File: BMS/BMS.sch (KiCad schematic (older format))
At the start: 77 parts, among them J1 Cell Taps, J10 Current Sensor, J2 IsoSPI, J3 Temp 1, J4 Temp 2, J5 Temp 3, J6 Temp 4, J7 Temp 5, J8 Temp 6, J9 Temp 7, Q1 NSV1C201MZ4, Q2 BSS308PE, Q3 BSS308PE, Q4 BSS308PE, Q5 BSS308PE, Q6 BSS308PE, Q7 BSS308PE, Q8 BSS308PE, SW1 SW_DIP_x04, U1 LTC6811, U2 ADG708

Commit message: Begin work on BMS schematic
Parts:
- U1: symbol BMS-rescue:LTC6811-FS_FINAL -> FS_FINAL:LTC6811
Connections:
- wire segments 233 -> 230
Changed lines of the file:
@@
 EESchema Schematic File Version 4
-LIBS:symbols
-LIBS:arduino
-LIBS:FS FINAL
-LIBS:BMS-cache
 EELAYER 26 0
 EELAYER END
@@
 $EndDescr
 $Comp
-L BMS-rescue:LTC6811-FS_FINAL U1
+L FS_FINAL:LTC6811 U1
 U 1 1 5C45220C
 P 5800 1100
@@
 	6500 3200 7100 3200
 Wire Wire Line
-	7500 3500 7100 3500
-Wire Wire Line
 	6500 3100 7500 3100
 Wire Wire Line
@@
 Wire Wire Line
 	5000 3900 5000 6750
-Wire Wire Line
-	7600 3500 7500 3500
-Connection ~ 7500 3500
 Text GLabel 5100 6750 2    50   Output ~ 0
 V-
@@
 Wire Wire Line
 	7950 2150 7850 2150
-Connection ~ 7850 2150
 Text GLabel 7700 4350 0    50   Input ~ 0
 MUX_A0
@@
 Text GLabel 8500 5350 2    50   Output ~ 0
 TEMP
-Wire Wire Line
-	8850 2250 8950 2250
-Wire Wire Line
-	8850 2850 8950 2850
-Connection ~ 8950 2250
-Connection ~ 8950 2850
 $Comp
 L FS_FINAL:HM2113ZNL L1
@@
 	1    0    0    -1
 $EndComp
-Wire Wire Line
-	8950 2250 9150 2250
-Wire Wire Line
-	8950 2850 9150 2850
 Wire Wire Line
 	9150 2250 9150 2450
@@
 Wire Wire Line
 	10450 2650 10250 2650
+Wire Wire Line
+	7100 3500 7600 3500
+Wire Wire Line
+	8850 2250 9150 2250
+Wire Wire Line
+	8850 2850 9150 2850
 $EndSCHEMATC

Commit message: BMS again
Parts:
- C13, C14: value 1uF -> 10nF
- R17: value 1M -> 10k
- R33, R34, R35, R36, R37, R38, R39: value R -> 10k
- SW1: footprint Buttons_Switches_SMD:SW_DIP_x4_W8.61mm_Slide_LowProfile -> FSFootprints:DIP A6H-4101
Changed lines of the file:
@@
 EESchema Schematic File Version 4
+LIBS:BMS-cache
 EELAYER 26 0
 EELAYER END
@@
 F 0 "SW1" H 10300 1617 50  0000 C CNN
 F 1 "SW_DIP_x04" H 10300 1526 50  0000 C CNN
-F 2 "Buttons_Switches_SMD:SW_DIP_x4_W8.61mm_Slide_LowProfile" H 10300 1150 50  0001 C CNN
-F 3 "" H 10300 1150 50  0001 C CNN
+F 2 "FSFootprints:DIP A6H-4101" H 10300 1150 50  0001 C CNN
+F 3 "https://omronfs.omron.com/en_US/ecb/products/pdf/en-a6h.pdf" H 10300 1150 50  0001 C CNN
 	1    10300 1150
 	1    0    0    -1
@@
 P 6650 2800
 F 0 "R17" V 6750 2800 50  0000 C CNN
-F 1 "1M" V 6650 2800 50  0000 C CNN
+F 1 "10k" V 6650 2800 50  0000 C CNN
 F 2 "Resistors_SMD:R_0805_HandSoldering" V 6580 2800 50  0001 C CNN
 F 3 "~" H 6650 2800 50  0001 C CNN
@@
 P 6100 4600
 F 0 "R34" H 6030 4554 50  0000 R CNN
-F 1 "R" H 6030 4645 50  0000 R CNN
+F 1 "10k" H 6030 4645 50  0000 R CNN
 F 2 "Resistors_SMD:R_0805_HandSoldering" V 6030 4600 50  0001 C CNN
 F 3 "~" H 6100 4600 50  0001 C CNN
@@
 P 6300 4600
 F 0 "R35" H 6230 4554 50  0000 R CNN
-F 1 "R" H 6230 4645 50  0000 R CNN
+F 1 "10k" H 6230 4645 50  0000 R CNN
 F 2 "Resistors_SMD:R_0805_HandSoldering" V 6230 4600 50  0001 C CNN
 F 3 "~" H 6300 4600 50  0001 C CNN
@@
 P 6500 4600
 F 0 "R36" H 6430 4554 50  0000 R CNN
-F 1 "R" H 6430 4645 50  0000 R CNN
+F 1 "10k" H 6430 4645 50  0000 R CNN
 F 2 "Resistors_SMD:R_0805_HandSoldering" V 6430 4600 50  0001 C CNN
 F 3 "~" H 6500 4600 50  0001 C CNN
@@
 P 6700 4600
 F 0 "R37" H 6630 4554 50  0000 R CNN
-F 1 "R" H 6630 4645 50  0000 R CNN
+F 1 "10k" H 6630 4645 50  0000 R CNN
 F 2 "Resistors_SMD:R_0805_HandSoldering" V 6630 4600 50  0001 C CNN
 F 3 "~" H 6700 4600 50  0001 C CNN
@@
 P 5900 4600
 F 0 "R33" H 5830 4554 50  0000 R CNN
-F 1 "R" H 5830 4645 50  0000 R CNN
+F 1 "10k" H 5830 4645 50  0000 R CNN
 F 2 "Resistors_SMD:R_0805_HandSoldering" V 5830 4600 50  0001 C CNN
 F 3 "~" H 5900 4600 50  0001 C CNN
@@
 P 6900 4600
 F 0 "R38" H 6830 4554 50  0000 R CNN
-F 1 "R" H 6830 4645 50  0000 R CNN
+F 1 "10k" H 6830 4645 50  0000 R CNN
 F 2 "Resistors_SMD:R_0805_HandSoldering" V 6830 4600 50  0001 C CNN
 F 3 "~" H 6900 4600 50  0001 C CNN
@@
 P 7100 4600
 F 0 "R39" H 7030 4554 50  0000 R CNN
-F 1 "R" H 7030 4645 50  0000 R CNN
+F 1 "10k" H 7030 4645 50  0000 R CNN
 F 2 "Resistors_SMD:R_0805_HandSoldering" V 7030 4600 50  0001 C CNN
 F 3 "~" H 7100 4600 50  0001 C CNN
@@
 P 9250 3050
 F 0 "C13" V 9350 3050 50  0000 C CNN
-F 1 "1uF" V 9150 3050 50  0000 C CNN
+F 1 "10nF" V 9150 3050 50  0000 C CNN
 F 2 "Capacitors_SMD:C_0805_HandSoldering" H 9288 2900 50  0001 C CNN
 F 3 "~" H 9250 3050 50  0001 C CNN
@@
 P 10350 3050
 F 0 "C14" V 10450 3050 50  0000 C CNN
-F 1 "1uF" V 10250 3050 50  0000 C CNN
+F 1 "10nF" V 10250 3050 50  0000 C CNN
 F 2 "Capacitors_SMD:C_0805_HandSoldering" H 10388 2900 50  0001 C CNN
 F 3 "~" H 10350 3050 50  0001 C CNN

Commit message: BMS board v0.1
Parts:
- removed J10: Current Sensor, Connectors_Molex:Molex_NanoFit_1x03x2.50mm_Straight, symbol Connector:Conn_01x03_Male
- J1: footprint FSFootprints:Cell Taps -> Connectors_Molex:Molex_NanoFit_1x08x2.50mm_Straight
- R17: value 10k -> 0
- U1: footprint Housings_SSOP:SSOP-48_7.5x15.9mm_Pitch0.635mm -> FSFootprints:FSOP-48_[LTC6811-2]
- U2: footprint Package_SO:TSSOP-16_4.4x5mm_P0.65mm -> Housings_SSOP:TSSOP-16_4.4x5mm_Pitch0.65mm
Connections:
- wire segments 230 -> 232
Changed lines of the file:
@@
 F 0 "U1" H 5800 1265 50  0000 C CNN
 F 1 "LTC6811" H 5800 1174 50  0000 C CNN
-F 2 "Housings_SSOP:SSOP-48_7.5x15.9mm_Pitch0.635mm" H 5800 1100 50  0001 C CNN
+F 2 "FSFootprints:FSOP-48_[LTC6811-2]" H 5800 1100 50  0001 C CNN
 F 3 "" H 5800 1100 50  0001 C CNN
 	1    5800 1100
@@
 F 0 "J1" H 906 1728 50  0000 C CNN
 F 1 "Cell Taps" V 700 1200 50  0000 C CNN
-F 2 "FSFootprints:Cell Taps" H 800 1250 50  0001 C CNN
+F 2 "Connectors_Molex:Molex_NanoFit_1x08x2.50mm_Straight" H 800 1250 50  0001 C CNN
 F 3 "~" H 800 1250 50  0001 C CNN
 	1    800  1250
@@
 	1    7100 3350
 	-1   0    0    1
-$EndComp
-$Comp
-L Device:R R17
-U 1 1 5C72E4D4
-P 6650 2800
-F 0 "R17" V 6750 2800 50  0000 C CNN
-F 1 "10k" V 6650 2800 50  0000 C CNN
-F 2 "Resistors_SMD:R_0805_HandSoldering" V 6580 2800 50  0001 C CNN
-F 3 "~" H 6650 2800 50  0001 C CNN
-	1    6650 2800
-	0    1    1    0
 $EndComp
 $Comp
@@
 Text GLabel 6500 2600 2    50   Input ~ 0
 VREG
-Text GLabel 6800 2800 2    50   Input ~ 0
-VREG
 Text GLabel 10800 950  2    50   Input ~ 0
 VREG
@@
 F 0 "U2" H 7800 5800 50  0000 L CNN
 F 1 "ADG708" H 7800 5700 50  0000 L CNN
-F 2 "Package_SO:TSSOP-16_4.4x5mm_P0.65mm" H 8350 4100 50  0001 L CNN
+F 2 "Housings_SSOP:TSSOP-16_4.4x5mm_Pitch0.65mm" H 8350 4100 50  0001 L CNN
 F 3 "https://www.analog.com/media/en/technical-documentation/data-sheets/ADG708_709.pdf" H 8110 4950 50  0001 C CNN
 	1    8100 4950
@@
 V-
 Text GLabel 5750 6150 2    50   Input ~ 0
-V-
-Text GLabel 7700 5550 0    50   Input ~ 0
 V-
 $Comp
@@
 Text GLabel 9250 3150 3    50   Input ~ 0
 V-
-$Comp
-L Connector:Conn_01x03_Male J10
-U 1 1 5C7A9370
-P 9800 3700
-F 0 "J10" H 9773 3723 50  0000 R CNN
-F 1 "Current Sensor" H 9773 3632 50  0000 R CNN
-F 2 "Connectors_Molex:Molex_NanoFit_1x03x2.50mm_Straight" H 9800 3700 50  0001 C CNN
-F 3 "~" H 9800 3700 50  0001 C CNN
-	1    9800 3700
-	-1   0    0    -1
-$EndComp
-Text GLabel 9600 3600 0    50   Input ~ 0
-VREG
-Text GLabel 9600 3800 0    50   Input ~ 0
-V-
-Wire Wire Line
-	9600 3700 6500 3700
 Text GLabel 7700 4650 0    50   Input ~ 0
 VREG
@@
 Text GLabel 7700 4550 0    50   Input ~ 0
 MUX_A2
-Text GLabel 6500 3400 2    50   Output ~ 0
+Text GLabel 6500 3500 2    50   Output ~ 0
 MUX_A0
-Text GLabel 6500 3500 2    50   Output ~ 0
+Text GLabel 6500 3800 2    50   Output ~ 0
 MUX_A1
-Text GLabel 6500 3600 2    50   Output ~ 0
+Text GLabel 6500 3700 2    50   Output ~ 0
 MUX_A2
-Text GLabel 6500 3800 2    50   Input ~ 0
+Text GLabel 6500 3400 2    50   Input ~ 0
 TEMP
 Text GLabel 8500 5350 2    50   Output ~ 0
@@
 	10450 2650 10250 2650
 Wire Wire Line
-	7100 3500 7600 3500
-Wire Wire Line
-	8850 2250 9150 2250
-Wire Wire Line
-	8850 2850 9150 2850
+	7100 3500 7500 3500
+Wire Wire Line
+	8850 2250 8950 2250
+Wire Wire Line
+	8850 2850 8950 2850
+Connection ~ 7500 3500
+Wire Wire Line
+	7500 3500 7600 3500
+Connection ~ 8950 2250
+Wire Wire Line
+	8950 2250 9150 2250
+Connection ~ 8950 2850
+Wire Wire Line
+	8950 2850 9150 2850
+Connection ~ 7850 2150
+Text GLabel 6500 3600 2    50   Input ~ 0
+VREG
+$Comp
+L Device:R R17
+U 1 1 5C80812D
+P 8200 850
+F 0 "R17" V 7993 850 50  0000 C CNN
+F 1 "0" V 8084 850 50  0000 C CNN
+F 2 "Resistors_SMD:R_0805_HandSoldering" V 8130 850 50  0001 C CNN
+F 3 "~" H 8200 850 50  0001 C CNN
+	1    8200 850
+	0    1    1    0
+$EndComp
+Text GLabel 8050 850  0    50   Output ~ 0
+VREG
+Text GLabel 8350 850  2    50   Output ~ 0
+VREG
 $EndSCHEMATC

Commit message: yikes
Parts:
- removed C14: 10nF, Capacitors_SMD:C_0805_HandSoldering, symbol Device:C_Small
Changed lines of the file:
@@
 Wire Wire Line
 	9250 2550 9350 2550
-$Comp
-L Device:R R40
-U 1 1 5CA16E1A
-P 10600 2450
-F 0 "R40" V 10700 2400 50  0000 L CNN
-F 1 "22" V 10600 2450 50  0000 C CNN
-F 2 "Resistors_SMD:R_0805_HandSoldering" V 10530 2450 50  0001 C CNN
-F 3 "~" H 10600 2450 50  0001 C CNN
-	1    10600 2450
-	0    1    -1   0
-$EndComp
-$Comp
-L Device:R R41
-U 1 1 5CA1723F
-P 10600 2650
-F 0 "R41" V 10700 2600 50  0000 L CNN
-F 1 "22" V 10600 2650 50  0000 C CNN
-F 2 "Resistors_SMD:R_0805_HandSoldering" V 10530 2650 50  0001 C CNN
-F 3 "~" H 10600 2650 50  0001 C CNN
-	1    10600 2650
-	0    1    -1   0
-$EndComp
 Wire Wire Line
 	10750 2450 10850 2450
@@
 Wire Wire Line
 	10850 2650 10750 2650
-$Comp
-L Device:C_Small C14
-U 1 1 5CA52F72
-P 10350 3050
-F 0 "C14" V 10450 3050 50  0000 C CNN
-F 1 "10nF" V 10250 3050 50  0000 C CNN
-F 2 "Capacitors_SMD:C_0805_HandSoldering" H 10388 2900 50  0001 C CNN
-F 3 "~" H 10350 3050 50  0001 C CNN
-	1    10350 3050
-	1    0    0    -1
-$EndComp
-Text GLabel 10350 3150 3    50   Input ~ 0
-V-
-Wire Wire Line
-	10350 2950 10350 2550
-Wire Wire Line
-	10250 2550 10350 2550
 Wire Wire Line
 	10250 2450 10450 2450
@@
 Text GLabel 8350 850  2    50   Output ~ 0
 VREG
+$Comp
+L Device:R R41
+U 1 1 5CA1723F
+P 10600 2650
+F 0 "R41" V 10700 2600 50  0000 L CNN
+F 1 "22" V 10600 2650 50  0000 C CNN
+F 2 "Resistors_SMD:R_0805_HandSoldering" V 10530 2650 50  0001 C CNN
+F 3 "~" H 10600 2650 50  0001 C CNN
+	1    10600 2650
+	0    1    -1   0
+$EndComp
+$Comp
+L Device:R R40
+U 1 1 5CA16E1A
+P 10600 2450
+F 0 "R40" V 10700 2400 50  0000 L CNN
+F 1 "22" V 10600 2450 50  0000 C CNN
+F 2 "Resistors_SMD:R_0805_HandSoldering" V 10530 2450 50  0001 C CNN
+F 3 "~" H 10600 2450 50  0001 C CNN
+	1    10600 2450
+	0    1    -1   0
+$EndComp
 $EndSCHEMATC

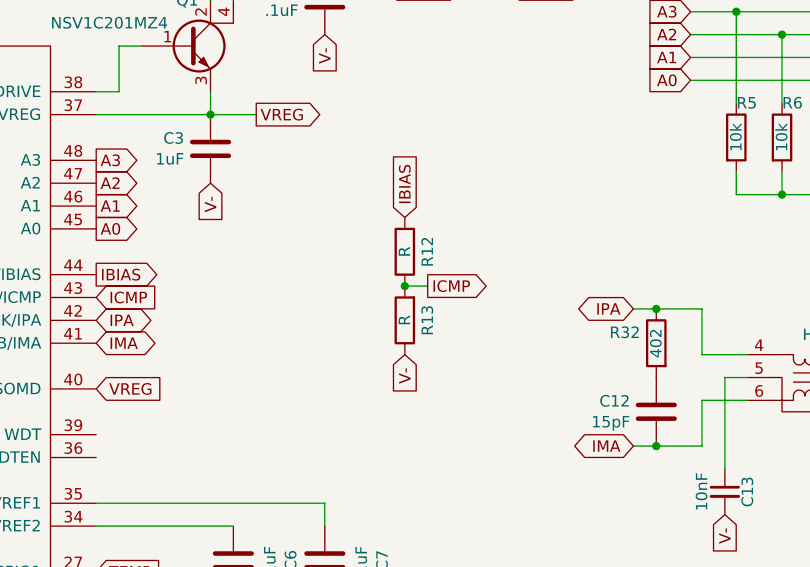
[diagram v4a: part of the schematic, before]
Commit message: Update BMS bias resistors and enable pin
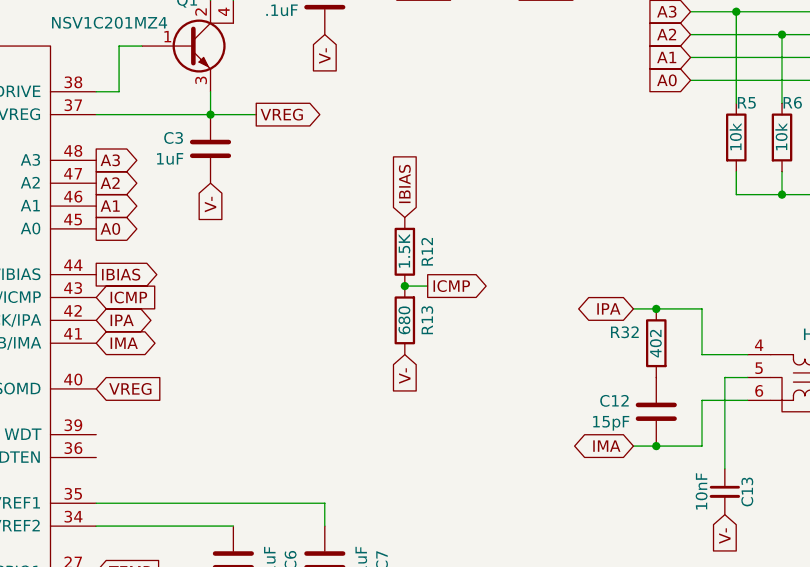
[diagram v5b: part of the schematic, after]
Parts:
- R12: value R -> 1.5K
- R13: value R -> 680
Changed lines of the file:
@@
 P 7850 2000
 F 0 "R12" V 7750 2000 50  0000 C CNN
-F 1 "R" V 7850 2000 50  0000 C CNN
+F 1 "1.5K" V 7850 2000 50  0000 C CNN
 F 2 "Resistors_SMD:R_0805_HandSoldering" V 7780 2000 50  0001 C CNN
 F 3 "~" H 7850 2000 50  0001 C CNN
@@
 P 7850 2300
 F 0 "R13" V 7750 2300 50  0000 C CNN
-F 1 "R" V 7850 2300 50  0000 C CNN
+F 1 "680" V 7850 2300 50  0000 C CNN
 F 2 "Resistors_SMD:R_0805_HandSoldering" V 7780 2300 50  0001 C CNN
 F 3 "~" H 7850 2300 50  0001 C CNN
